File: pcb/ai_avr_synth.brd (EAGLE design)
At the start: 99.1 x 69.8 mm, 45 parts, among them IC1 ATMEGA328P-PDIP, J1 1X02ST, J2 1X06, J3 1X08, J4 1X08, J5 MIDIJACK, J6 STEREOJACKSJ1-3555NG, U1 MC7805, U2 TLC2262, U3 6N138

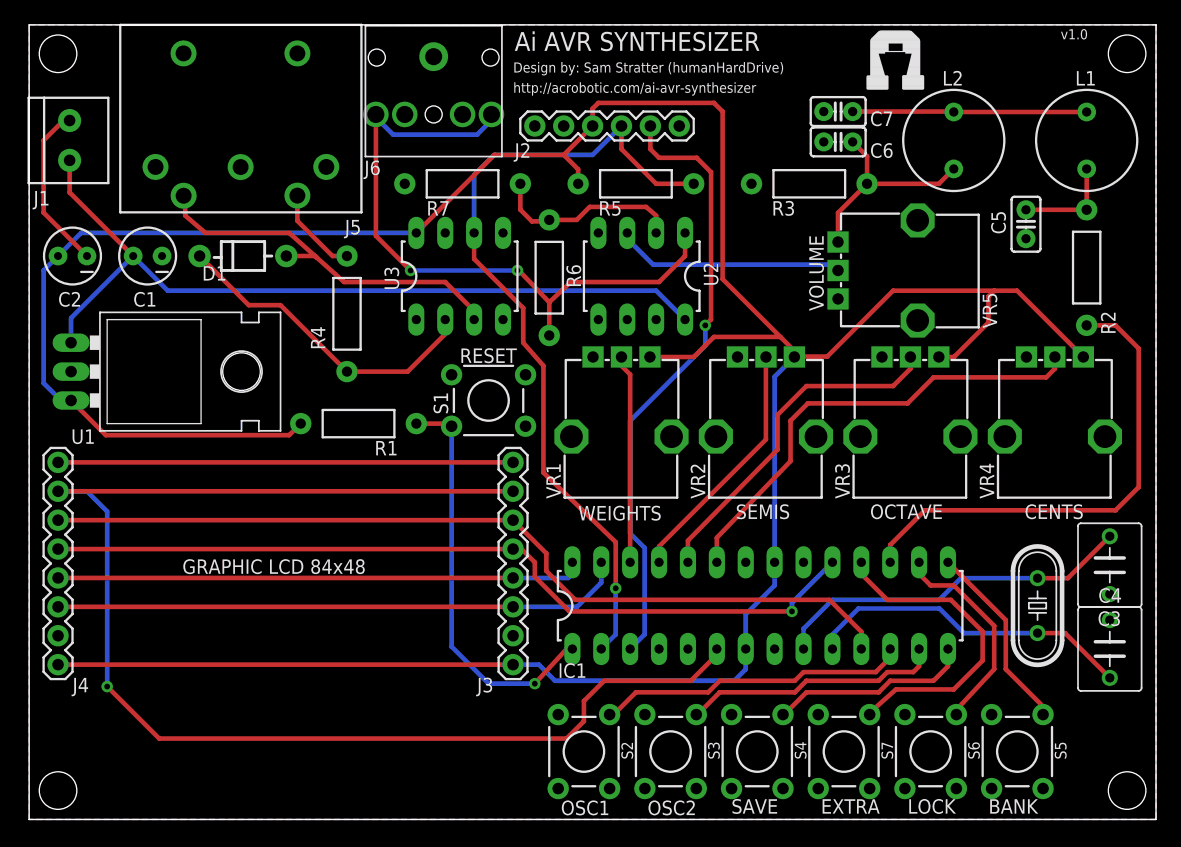
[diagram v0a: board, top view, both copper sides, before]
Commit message: Revisions on LCD orientation, and positioning of switches/pots.
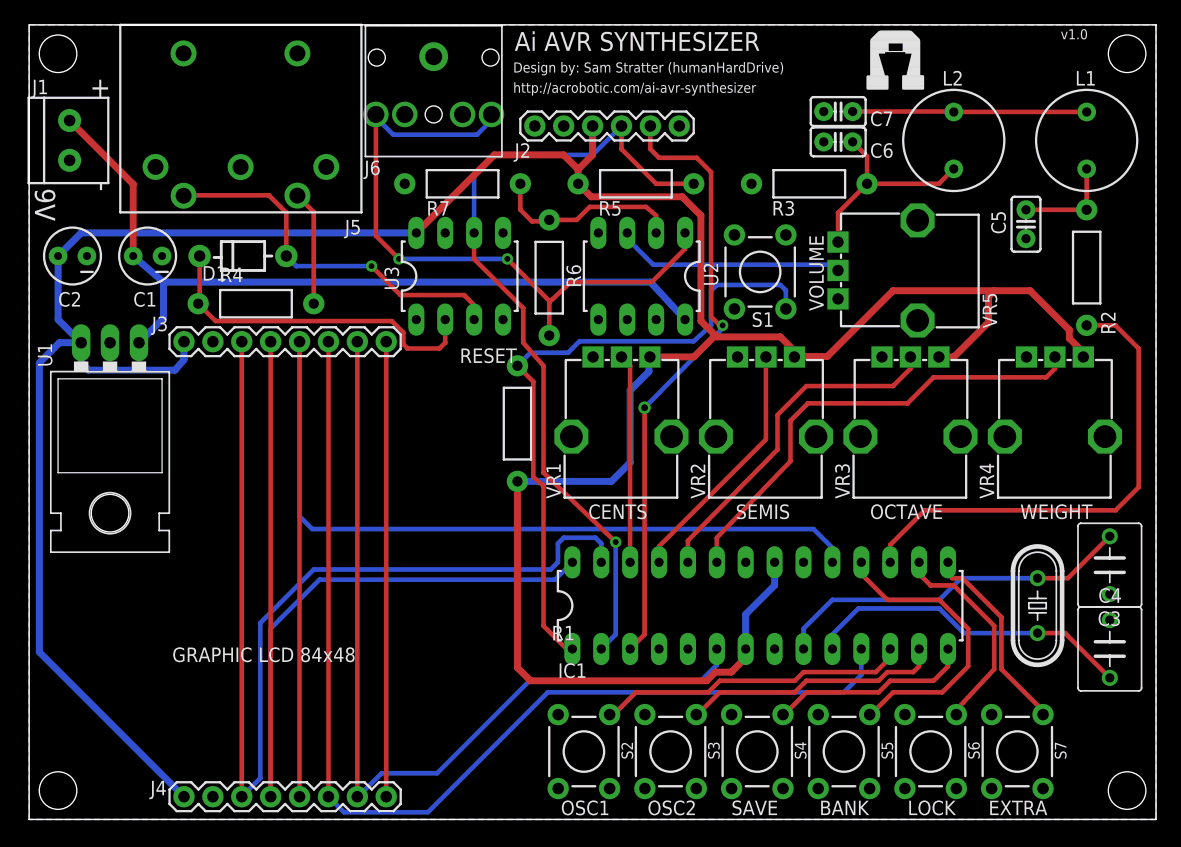
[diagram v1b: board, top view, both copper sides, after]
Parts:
- moved J4 28.6 mm to (22.5, 2.00), turned to 0 degrees
- moved J3 28.0 mm to (22.5, 42.0), turned to 0 degrees
- moved S1 26.4 mm to (64.3, 48.1), turned to 90 degrees
- moved S5 15.2 mm to (71.6, 5.97)
- moved S7 15.2 mm to (86.9, 5.97)
- moved R1 14.0 mm to (42.9, 34.8), turned to 270 degrees
- moved R4 8.05 mm to (19.9, 45.3), turned to 0 degrees
- moved U1 5.69 mm to (7.11, 34.9), turned to 180 degrees
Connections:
- net 9V: now also J1.1; no longer J1.2
- net BTN_BANK: now also IC1.18; no longer IC1.15
- net BTN_EXTRA: now also IC1.15; no longer IC1.18
- net CENTS: now also IC1.26, VR1.P$2; no longer IC1.23, VR4.P$2
- net GND: now also J1.2; no longer J1.1
- net WEIGHT: now also IC1.23, VR4.P$2; no longer IC1.26, VR1.P$2
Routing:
- net LCD_SCK: track 120.5 -> 77.8 mm, vias 1 -> 0
- net LCD_SCE: track 50.4 -> 91.5 mm
- net LCD_RST: track 46.4 -> 83.7 mm
- net LCD_DC: track 73.3 -> 104.6 mm, vias 1 -> 0
- net CENTS: track 41.2 -> 18.4 mm
- net WEIGHT: track 18.4 -> 41.2 mm
- net RESET: track 35.9 -> 57.3 mm, vias 1 -> 0
- net LCD_SIN: track 77.1 -> 94.7 mm
- net GND: track 14.7 -> 0.00 mm
- net BTN_EXTRA: track 28.2 -> 17.4 mm
- net BTN_BANK: track 16.8 -> 26.1 mm
- net N$8: track 7.86 -> 10.1 mm
- net N$9: track 28.4 -> 30.4 mm
- net 5V: track 270.8 -> 269.6 mm
- net N$10: track 34.0 -> 33.0 mm, vias 0 -> 1
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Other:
- board text added: "+"
- board text added: "-"
- board text added: "9V"
- board text added: "WEIGHT"
- board text removed: "WEIGHTS"

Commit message: Adding gerbers, firmware. Updated README and index.
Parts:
- moved C3 0.25 mm to (95.0, 22.6), turned to 270 degrees
- moved R4 0.25 mm to (20.2, 45.3), turned to 180 degrees
- turned C4 to 90 degrees
- turned R5 to 0 degrees
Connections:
- removed net N$2: C3.2, IC1.9, XL1.2
- removed net N$8: J5.4, R4.P$2
- new net N$1: J5.4, R4.P$1
- new net N$4: C3.1, IC1.9, XL1.2
- net 5V: now also R5.P$1; no longer R5.P$2
- net GND: now also C3.2, C4.2; no longer C3.1, C4.1
- net N$3: now also C4.1; no longer C4.2
- net N$9: now also R4.P$2; no longer R4.P$1
- net RXI: now also R5.P$2; no longer R5.P$1
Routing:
- net N$4: track 0.00 -> 32.2 mm
- net N$2: track 32.1 -> 0.00 mm
- net N$1: track 0.00 -> 10.2 mm
- net N$8: track 10.1 -> 0.00 mm
- net GND: track 0.00 -> 2.54 mm

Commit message: Finalized BOM.
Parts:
- moved U$5 13.9 mm to (63.5, 60.6)
- moved J2 4.06 mm to (50.8, 65.0)
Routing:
- net RXI: track 71.7 -> 81.1 mm
- net TXO: track 54.0 -> 58.1 mm
- net 5V: track 269.9 -> 273.9 mm
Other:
- board text removed: "http://acrobotic.com/ai-avr-synthesizer"
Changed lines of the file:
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@@
 <wire x1="99.06" y1="69.85" x2="0" y2="69.85" width="0.127" layer="20"/>
 <wire x1="0" y1="69.85" x2="0" y2="0" width="0.127" layer="20"/>
-<text x="42.545" y="63.881" size="0.889" layer="21" font="vector" ratio="15">http://acrobotic.com/ai-avr-synthesizer</text>
-<text x="37.846" y="40.132" size="1.27" layer="21" font="vector" ratio="15">RESET</text>
-<text x="12.573" y="13.843" size="1.27" layer="21" font="vector" ratio="15">GRAPHIC LCD 84x48 </text>
+<text x="61.595" y="52.705" size="1.27" layer="21" font="vector" ratio="15">RESET</text>
+<text x="13.081" y="16.129" size="1.27" layer="21" font="vector" ratio="15">GRAPHIC LCD 84x48 </text>
 <text x="69.85" y="44.704" size="1.27" layer="21" font="vector" ratio="15" rot="R90">VOLUME</text>
-<text x="49.149" y="26.416" size="1.27" layer="21" font="vector" ratio="15">CENTS</text>
-<text x="62.103" y="26.416" size="1.27" layer="21" font="vector" ratio="15">SEMIS</text>
-<text x="73.914" y="26.416" size="1.27" layer="21" font="vector" ratio="15">OCTAVE</text>
-<text x="87.122" y="26.416" size="1.27" layer="21" font="vector" ratio="15">WEIGHT</text>
-<text x="42.672" y="67.564" size="1.651" layer="21" font="vector" ratio="15">Ai AVR SYNTHESIZER</text>
-<text x="90.678" y="68.58" size="0.889" layer="21" font="vector" ratio="15">v1.0</text>
-<text x="42.545" y="65.659" size="0.889" layer="21" font="vector" ratio="15">Design by: Sam Stratter (humanHardDrive)</text>
+<text x="49.149" y="26.67" size="1.27" layer="21" font="vector" ratio="15">CENTS</text>
+<text x="62.103" y="26.67" size="1.27" layer="21" font="vector" ratio="15">SEMIS</text>
+<text x="73.914" y="26.67" size="1.27" layer="21" font="vector" ratio="15">OCTAVE</text>
+<text x="86.995" y="26.67" size="1.27" layer="21" font="vector" ratio="15">WEIGHT</text>
+<text x="59.69" y="67.31" size="1.651" layer="21" font="vector" ratio="15">Ai AVR SYNTHESIZER</text>
+<text x="90.297" y="68.199" size="0.889" layer="21" font="vector" ratio="15">v1.0</text>
+<text x="59.563" y="65.405" size="0.889" layer="21" font="vector" ratio="15">Design by: Sam Stratter (humanHardDrive)</text>
 <text x="46.736" y="0.381" size="1.27" layer="21" font="vector" ratio="15">OSC1</text>
 <text x="54.356" y="0.381" size="1.27" layer="21" font="vector" ratio="15">OSC2</text>
@@
 </autorouter>
 <elements>
-<element name="U$5" library="Ai_Miscellany" package="AI-LOGO-L" value="AI-LOGOL" x="76.2" y="66.294"/>
+<element name="U$5" library="Ai_Miscellany" package="AI-LOGO-L" value="AI-LOGOL" x="63.5" y="60.579"/>
 <element name="U1" library="Ai_Power" package="TO220" value="MC7805" x="7.112" y="34.925" smashed="yes" rot="R180">
-<attribute name="NAME" x="0.762" y="41.91" size="1.27" layer="25" font="vector" ratio="15" rot="R270"/>
+<attribute name="NAME" x="1.016" y="39.751" size="1.27" layer="25" font="vector" ratio="15"/>
 </element>
 <element name="C1" library="Ai_Passives" package="CAP-POL-025X50" value="4.7uF" x="10.414" y="49.53" smashed="yes" rot="R180">
@@
 <attribute name="NAME" x="0.254" y="63.754" size="1.27" layer="25" font="vector" ratio="15"/>
 </element>
-<element name="J2" library="Ai_Connectors" package="1X06" value="1X06" x="50.8" y="60.96" smashed="yes">
-<attribute name="NAME" x="42.672" y="58.166" size="1.27" layer="25" font="vector" ratio="15"/>
+<element name="J2" library="Ai_Connectors" package="1X06" value="1X06" x="50.8" y="65.024" smashed="yes">
+<attribute name="NAME" x="42.672" y="62.23" size="1.27" layer="25" font="vector" ratio="15"/>
 </element>
 <element name="J3" library="Ai_Connectors" package="1X08" value="1X08" x="22.5" y="42" smashed="yes">
@@
 <element name="XL1" library="Ai_Passives" package="CRYSTAL-HC49S" value="16MHz" x="88.646" y="18.796" rot="R90"/>
 <element name="C3" library="Ai_Passives" package="CAP-055X070" value="22pF" x="94.996" y="22.606" smashed="yes" rot="R270">
-<attribute name="NAME" x="93.98" y="26.67" size="1.27" layer="25" font="vector" ratio="15"/>
+<attribute name="NAME" x="95.758" y="26.543" size="1.27" layer="25" font="vector" ratio="15"/>
 </element>
 <element name="C4" library="Ai_Passives" package="CAP-055X070" value="22pF" x="94.996" y="14.986" smashed="yes" rot="R90">
-<attribute name="NAME" x="96.012" y="10.922" size="1.27" layer="25" font="vector" ratio="15" rot="R180"/>
+<attribute name="NAME" x="95.885" y="9.779" size="1.27" layer="25" font="vector" ratio="15"/>
 </element>
 <element name="C5" library="Ai_Passives" package="CAP-025X050" value=".047uF" x="87.63" y="52.324" smashed="yes" rot="R270">
@@
 </element>
 <element name="R3" library="Ai_Passives" package="RES-AXIAL-0.4" value="270" x="68.58" y="55.88" smashed="yes">
-<attribute name="NAME" x="65.278" y="53.086" size="1.27" layer="25" font="vector" ratio="15"/>
+<attribute name="NAME" x="69.088" y="53.213" size="1.27" layer="25" font="vector" ratio="15"/>
 </element>
 <element name="R4" library="Ai_Passives" package="RES-AXIAL-0.4" value="220" x="20.193" y="45.339" rot="R180"/>
@@
 </element>
 <element name="L1" library="Ai_Passives" package="RLB0912" value="4700uH" x="92.964" y="59.69" smashed="yes" rot="R90">
-<attribute name="NAME" x="91.948" y="64.516" size="1.27" layer="25" font="vector" ratio="15"/>
+<attribute name="NAME" x="96.647" y="62.992" size="1.27" layer="25" font="vector" ratio="15"/>
 </element>
 <element name="L2" library="Ai_Passives" package="RLB0912" value="4700uH" x="81.28" y="59.69" smashed="yes" rot="R270">
-<attribute name="NAME" x="80.264" y="64.516" size="1.27" layer="25" font="vector" ratio="15"/>
+<attribute name="NAME" x="84.836" y="62.992" size="1.27" layer="25" font="vector" ratio="15"/>
 </element>
 <element name="VR5" library="Ai_Passives" package="POT-09X09" value="10K" x="77.47" y="48.26" smashed="yes" rot="R180">
@@
 <wire x1="52.832" y1="31.369" x2="51.181" y2="29.718" width="0.6096" layer="16"/>
 <wire x1="51.181" y1="29.718" x2="42.926" y2="29.718" width="0.6096" layer="16"/>
-<wire x1="49.53" y1="60.96" x2="49.53" y2="58.42" width="0.6096" layer="1"/>
+<wire x1="49.53" y1="65.024" x2="49.53" y2="58.42" width="0.6096" layer="1"/>
 <wire x1="49.53" y1="58.42" x2="48.26" y2="57.15" width="0.6096" layer="1"/>
 <wire x1="49.403" y1="54.737" x2="57.404" y2="54.737" width="0.6096" layer="1"/>
@@
 <contactref element="U3" pad="6"/>
 <contactref element="J2" pad="4"/>
-<wire x1="52.07" y1="60.96" x2="52.07" y2="58.928" width="0.4064" layer="1"/>
+<wire x1="52.07" y1="65.024" x2="52.07" y2="58.928" width="0.4064" layer="1"/>
 <wire x1="52.07" y1="58.928" x2="55.118" y2="55.88" width="0.4064" layer="1"/>
-<wire x1="52.07" y1="60.96" x2="49.53" y2="58.42" width="0.4064" layer="16"/>
-<wire x1="49.53" y1="58.42" x2="40.894" y2="58.42" width="0.4064" layer="16"/>
+<wire x1="51.562" y1="58.42" x2="40.894" y2="58.42" width="0.4064" layer="16"/>
 <wire x1="40.894" y1="58.42" x2="39.116" y2="56.642" width="0.4064" layer="16"/>
 <wire x1="39.116" y1="56.642" x2="39.116" y2="51.562" width="0.4064" layer="16"/>
@@
 <contactref element="R5" pad="P$2"/>
 <wire x1="58.42" y1="55.88" x2="55.118" y2="55.88" width="0.4064" layer="1"/>
+<wire x1="51.562" y1="58.42" x2="52.07" y2="58.928" width="0.4064" layer="16"/>
+<wire x1="52.07" y1="58.928" x2="52.07" y2="65.024" width="0.4064" layer="16"/>
 </signal>
 <signal name="TXO">
 <contactref element="IC1" pad="3"/>
 <contactref element="J2" pad="5"/>
-<wire x1="54.61" y1="60.96" x2="54.61" y2="58.928" width="0.4064" layer="1"/>
+<wire x1="54.61" y1="65.024" x2="54.61" y2="58.928" width="0.4064" layer="1"/>
 <wire x1="54.61" y1="58.928" x2="55.372" y2="58.166" width="0.4064" layer="1"/>
 <wire x1="55.372" y1="58.166" x2="58.674" y2="58.166" width="0.4064" layer="1"/>

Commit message: Updating libraries
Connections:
- net 5V: now also C2.A; no longer C2.1
- net 9V: now also C1.A; no longer C1.1
- net GND: now also C1.C, C2.C; no longer C1.2, C2.2
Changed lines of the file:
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@@
 <contactref element="U2" pad="4"/>
 <contactref element="U1" pad="GND"/>
-<contactref element="C1" pad="2"/>
-<contactref element="C2" pad="2"/>
+<contactref element="C1" pad="C"/>
+<contactref element="C2" pad="C"/>
 <contactref element="S1" pad="B@1"/>
 <contactref element="IC1" pad="22"/>
@@
 <signal name="9V" class="1">
 <contactref element="U1" pad="IN"/>
-<contactref element="C1" pad="1"/>
+<contactref element="C1" pad="A"/>
 <contactref element="U2" pad="8"/>
 <wire x1="9.144" y1="49.53" x2="11.811" y2="47.244" width="0.6096" layer="16"/>
@@
 <signal name="5V" class="1">
 <contactref element="U1" pad="OUT"/>
-<contactref element="C2" pad="1"/>
+<contactref element="C2" pad="A"/>
 <contactref element="R1" pad="P$2"/>
 <contactref element="IC1" pad="7"/>

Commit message: changes to schematic fonts, and audiojack pad names
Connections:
- net GND: now also J6.GND; no longer J6.1
- net SND_OUT: now also J6.RNG, J6.TIP; no longer J6.2, J6.3
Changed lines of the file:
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@@
 <contactref element="R7" pad="P$1"/>
 <contactref element="U2" pad="4"/>
-<contactref element="J6" pad="1"/>
+<contactref element="J6" pad="GND"/>
 <contactref element="S7" pad="A@1"/>
 <contactref element="S6" pad="A@1"/>
@@
 <contactref element="R6" pad="P$2"/>
 <contactref element="U2" pad="1"/>
-<contactref element="J6" pad="3"/>
-<contactref element="J6" pad="2"/>
+<contactref element="J6" pad="RNG"/>
+<contactref element="J6" pad="TIP"/>
 <wire x1="32.512" y1="49.276" x2="30.48" y2="51.308" width="0.4064" layer="1"/>
 <wire x1="30.48" y1="51.308" x2="30.48" y2="61.976" width="0.4064" layer="1"/>
